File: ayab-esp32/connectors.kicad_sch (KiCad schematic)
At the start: 21 parts, among them J401 900_SOLENOIDS_A, J402 900_SOLENOIDS_B, J403 USER_I2C, J404 Conn_01x06, J405 910_SOLENOIDS_A, J406 910_SOLENOIDS_B, J407 910_ENCODERS_EOL_R, J408 USER_UART, J409 930_SOLENOIDS_A, J410 930_SOLENOIDS_B, J411 930_910_EOL_L, J412 930_EOL_R, J413 930_ENCODERS, J414 965_EOL_L, J415 965_EOL_R, J416 965_ENCODERS

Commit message: fix folder structure and update gitignore
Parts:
- J401, J405, J407, J409: symbol Connector_Generic:Conn_01x10 -> ayab-esp32:Conn_01x10
- J402, J406, J410: symbol Connector_Generic:Conn_01x08 -> ayab-esp32:Conn_01x08
- J403, J408: symbol Connector_Generic:Conn_01x04 -> ayab-esp32:Conn_01x04
- J404: symbol Connector_Generic:Conn_01x06 -> ayab-esp32:Conn_01x06
- J411, J412, J414, J415: symbol Connector_Generic:Conn_01x03 -> ayab-esp32:Conn_01x03
- J413, J416: symbol Connector_Generic:Conn_01x05 -> ayab-esp32:Conn_01x05
- R401, R402, R403: symbol Device:R_Small_US -> ayab-esp32:R_Small_US
- TP401, TP402: symbol Connector:TestPoint -> ayab-esp32:TestPoint
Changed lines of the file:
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@@
     )
   )
-  (symbol (lib_id "Device:R_Small_US") (at 49.53 172.72 0) (unit 1)
+  (symbol (lib_id "ayab-esp32:R_Small_US") (at 49.53 172.72 0) (unit 1)
     (in_bom yes) (on_board yes) (dnp no)
     (property "Reference" "R402" (at 46.99 171.45 0)
@@
     )
   )
-  (symbol (lib_id "Connector_Generic:Conn_01x04") (at 62.23 179.07 0) (unit 1)
+  (symbol (lib_id "ayab-esp32:Conn_01x04") (at 62.23 179.07 0) (unit 1)
     (in_bom yes) (on_board yes) (dnp no) (fields_autoplaced)
     (property "Reference" "J403" (at 64.77 179.07 0)
@@
     )
   )
-  (symbol (lib_id "Connector_Generic:Conn_01x05") (at 261.62 134.62 0) (mirror x) (unit 1)
+  (symbol (lib_id "ayab-esp32:Conn_01x05") (at 261.62 134.62 0) (mirror x) (unit 1)
     (in_bom yes) (on_board yes) (dnp no)
     (property "Reference" "J416" (at 264.16 133.35 0)
@@
     )
   )
-  (symbol (lib_id "Connector_Generic:Conn_01x03") (at 261.62 106.68 0) (unit 1)
+  (symbol (lib_id "ayab-esp32:Conn_01x03") (at 261.62 106.68 0) (unit 1)
     (in_bom yes) (on_board yes) (dnp no) (fields_autoplaced)
     (property "Reference" "J414" (at 264.16 105.41 0)
@@
     )
   )
-  (symbol (lib_id "Connector:TestPoint") (at 113.03 115.57 0) (unit 1)
+  (symbol (lib_id "ayab-esp32:TestPoint") (at 113.03 115.57 0) (unit 1)
     (in_bom yes) (on_board yes) (dnp no)
     (property "Reference" "TP402" (at 111.76 106.68 0)
@@
     )
   )
-  (symbol (lib_id "Connector_Generic:Conn_01x03") (at 193.04 106.68 0) (unit 1)
+  (symbol (lib_id "ayab-esp32:Conn_01x03") (at 193.04 106.68 0) (unit 1)
     (in_bom yes) (on_board yes) (dnp no) (fields_autoplaced)
     (property "Reference" "J411" (at 195.58 105.41 0)
@@
     )
   )
-  (symbol (lib_id "Connector_Generic:Conn_01x08") (at 121.92 76.2 0) (mirror x) (unit 1)
+  (symbol (lib_id "ayab-esp32:Conn_01x08") (at 121.92 76.2 0) (mirror x) (unit 1)
     (in_bom yes) (on_board yes) (dnp no)
     (property "Reference" "J406" (at 124.46 73.66 0)
@@
     )
   )
-  (symbol (lib_id "Device:R_Small_US") (at 39.37 172.72 0) (unit 1)
+  (symbol (lib_id "ayab-esp32:R_Small_US") (at 39.37 172.72 0) (unit 1)
     (in_bom yes) (on_board yes) (dnp no)
     (property "Reference" "R401" (at 36.83 171.45 0)
@@
     )
   )
-  (symbol (lib_id "Connector_Generic:Conn_01x10") (at 193.04 48.26 0) (mirror x) (unit 1)
+  (symbol (lib_id "ayab-esp32:Conn_01x10") (at 193.04 48.26 0) (mirror x) (unit 1)
     (in_bom yes) (on_board yes) (dnp no)
     (property "Reference" "J409" (at 195.58 45.72 0)
@@
     )
   )
-  (symbol (lib_id "Connector:TestPoint") (at 106.68 115.57 0) (unit 1)
+  (symbol (lib_id "ayab-esp32:TestPoint") (at 106.68 115.57 0) (unit 1)
     (in_bom yes) (on_board yes) (dnp no)
     (property "Reference" "TP401" (at 105.41 106.68 0)
@@
     )
   )
-  (symbol (lib_id "Connector_Generic:Conn_01x10") (at 121.92 48.26 0) (mirror x) (unit 1)
+  (symbol (lib_id "ayab-esp32:Conn_01x10") (at 121.92 48.26 0) (mirror x) (unit 1)
     (in_bom yes) (on_board yes) (dnp no)
     (property "Reference" "J405" (at 124.46 45.72 0)
@@
     )
   )
-  (symbol (lib_id "Connector_Generic:Conn_01x08") (at 54.61 76.2 0) (mirror x) (unit 1)
+  (symbol (lib_id "ayab-esp32:Conn_01x08") (at 54.61 76.2 0) (mirror x) (unit 1)
     (in_bom yes) (on_board yes) (dnp no)
     (property "Reference" "J402" (at 57.15 73.66 0)
@@
     )
   )
-  (symbol (lib_id "Connector_Generic:Conn_01x08") (at 193.04 76.2 0) (mirror x) (unit 1)
+  (symbol (lib_id "ayab-esp32:Conn_01x08") (at 193.04 76.2 0) (mirror x) (unit 1)
     (in_bom yes) (on_board yes) (dnp no)
     (property "Reference" "J410" (at 195.58 73.66 0)
@@
     )
   )
-  (symbol (lib_id "Device:R_Small_US") (at 93.98 171.45 0) (unit 1)
+  (symbol (lib_id "ayab-esp32:R_Small_US") (at 93.98 171.45 0) (unit 1)
     (in_bom yes) (on_board yes) (dnp no)
     (property "Reference" "R403" (at 91.44 170.18 0)
@@
     )
   )
-  (symbol (lib_id "Connector_Generic:Conn_01x10") (at 121.92 129.54 0) (mirror x) (unit 1)
+  (symbol (lib_id "ayab-esp32:Conn_01x10") (at 121.92 129.54 0) (mirror x) (unit 1)
     (in_bom yes) (on_board yes) (dnp no)
     (property "Reference" "J407" (at 124.46 137.16 0)
@@
     )
   )
-  (symbol (lib_id "Connector_Generic:Conn_01x10") (at 54.61 48.26 0) (mirror x) (unit 1)
+  (symbol (lib_id "ayab-esp32:Conn_01x10") (at 54.61 48.26 0) (mirror x) (unit 1)
     (in_bom yes) (on_board yes) (dnp no)
     (property "Reference" "J401" (at 57.15 45.72 0)
@@
     )
   )
-  (symbol (lib_id "Connector_Generic:Conn_01x05") (at 193.04 134.62 0) (mirror x) (unit 1)
+  (symbol (lib_id "ayab-esp32:Conn_01x05") (at 193.04 134.62 0) (mirror x) (unit 1)
     (in_bom yes) (on_board yes) (dnp no)
     (property "Reference" "J413" (at 195.58 133.35 0)
@@
     )
   )
-  (symbol (lib_id "Connector_Generic:Conn_01x03") (at 261.62 119.38 0) (unit 1)
+  (symbol (lib_id "ayab-esp32:Conn_01x03") (at 261.62 119.38 0) (unit 1)
     (in_bom yes) (on_board yes) (dnp no) (fields_autoplaced)
     (property "Reference" "J415" (at 264.16 118.11 0)
@@
     )
   )
-  (symbol (lib_id "Connector_Generic:Conn_01x06") (at 105.41 177.8 0) (unit 1)
+  (symbol (lib_id "ayab-esp32:Conn_01x06") (at 105.41 177.8 0) (unit 1)
     (in_bom yes) (on_board yes) (dnp no) (fields_autoplaced)
     (property "Reference" "J404" (at 107.95 177.8 0)
@@
     )
   )
-  (symbol (lib_id "Connector_Generic:Conn_01x03") (at 193.04 119.38 0) (unit 1)
+  (symbol (lib_id "ayab-esp32:Conn_01x03") (at 193.04 119.38 0) (unit 1)
     (in_bom yes) (on_board yes) (dnp no) (fields_autoplaced)
     (property "Reference" "J412" (at 195.58 118.11 0)
@@
     )
   )
-  (symbol (lib_id "Connector_Generic:Conn_01x04") (at 149.86 175.26 0) (unit 1)
+  (symbol (lib_id "ayab-esp32:Conn_01x04") (at 149.86 175.26 0) (unit 1)
     (in_bom yes) (on_board yes) (dnp no) (fields_autoplaced)
     (property "Reference" "J408" (at 152.4 175.26 0)

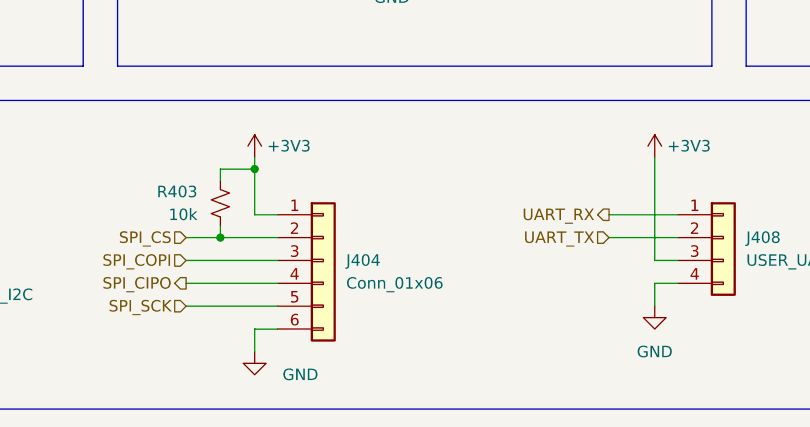
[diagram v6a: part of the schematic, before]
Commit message: fix comparator bias and hysteresis
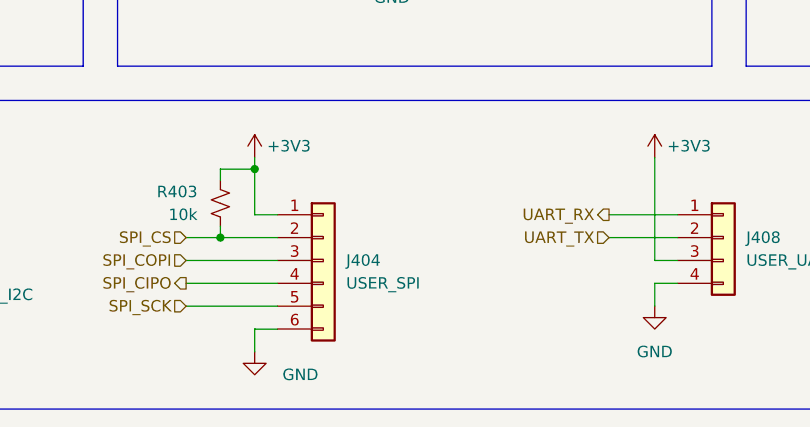
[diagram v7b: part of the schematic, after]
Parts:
- J404: value Conn_01x06 -> USER_SPI
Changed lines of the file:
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@@
       (effects (font (size 1.27 1.27)) (justify left))
     )
-    (property "Value" "Conn_01x06" (at 107.95 180.34 0)
+    (property "Value" "USER_SPI" (at 107.95 180.34 0)
       (effects (font (size 1.27 1.27)) (justify left))
     )

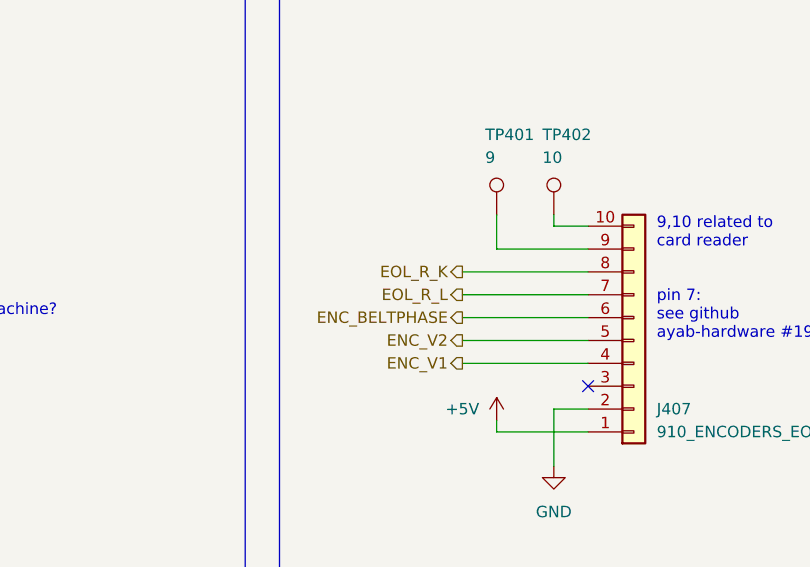
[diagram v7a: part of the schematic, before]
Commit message: refactor for i2c expander
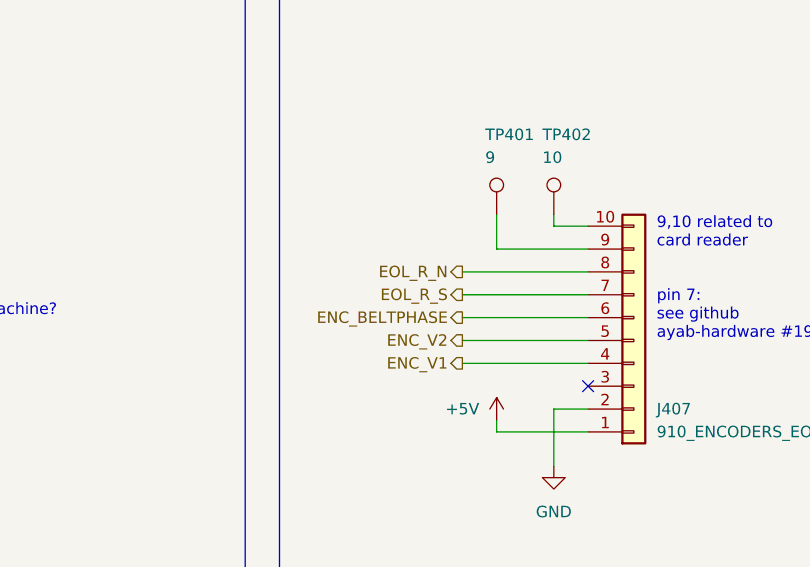
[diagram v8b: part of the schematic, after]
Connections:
- net EOL_R_K renamed EOL_R_N
- net EOL_R_L renamed EOL_R_S
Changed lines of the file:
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@@
     (effects (font (size 1.27 1.27)) (justify right))
   )
-  (hierarchical_label "EOL_R_K" (shape output) (at 102.87 121.92 180) (fields_autoplaced)
+  (hierarchical_label "EOL_R_N" (shape output) (at 102.87 121.92 180) (fields_autoplaced)
     (effects (font (size 1.27 1.27)) (justify right))
   )
@@
     (effects (font (size 1.27 1.27)) (justify right))
   )
-  (hierarchical_label "EOL_R_L" (shape output) (at 102.87 124.46 180) (fields_autoplaced)
+  (hierarchical_label "EOL_R_S" (shape output) (at 102.87 124.46 180) (fields_autoplaced)
     (effects (font (size 1.27 1.27)) (justify right))
   )
